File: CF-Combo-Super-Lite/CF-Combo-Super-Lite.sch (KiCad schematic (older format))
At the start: 21 parts, among them J1 IDE_CONNECTOR, J2 CF Adapter Power, J3 Jumpers, J4 Bus_ISA_8bit, U1 BIOS FLASH, U2 74HCT245, U3 GAL22V10, U4 DS1315, U5 AS6C4008-55PCN, Y1 32.768 KHz

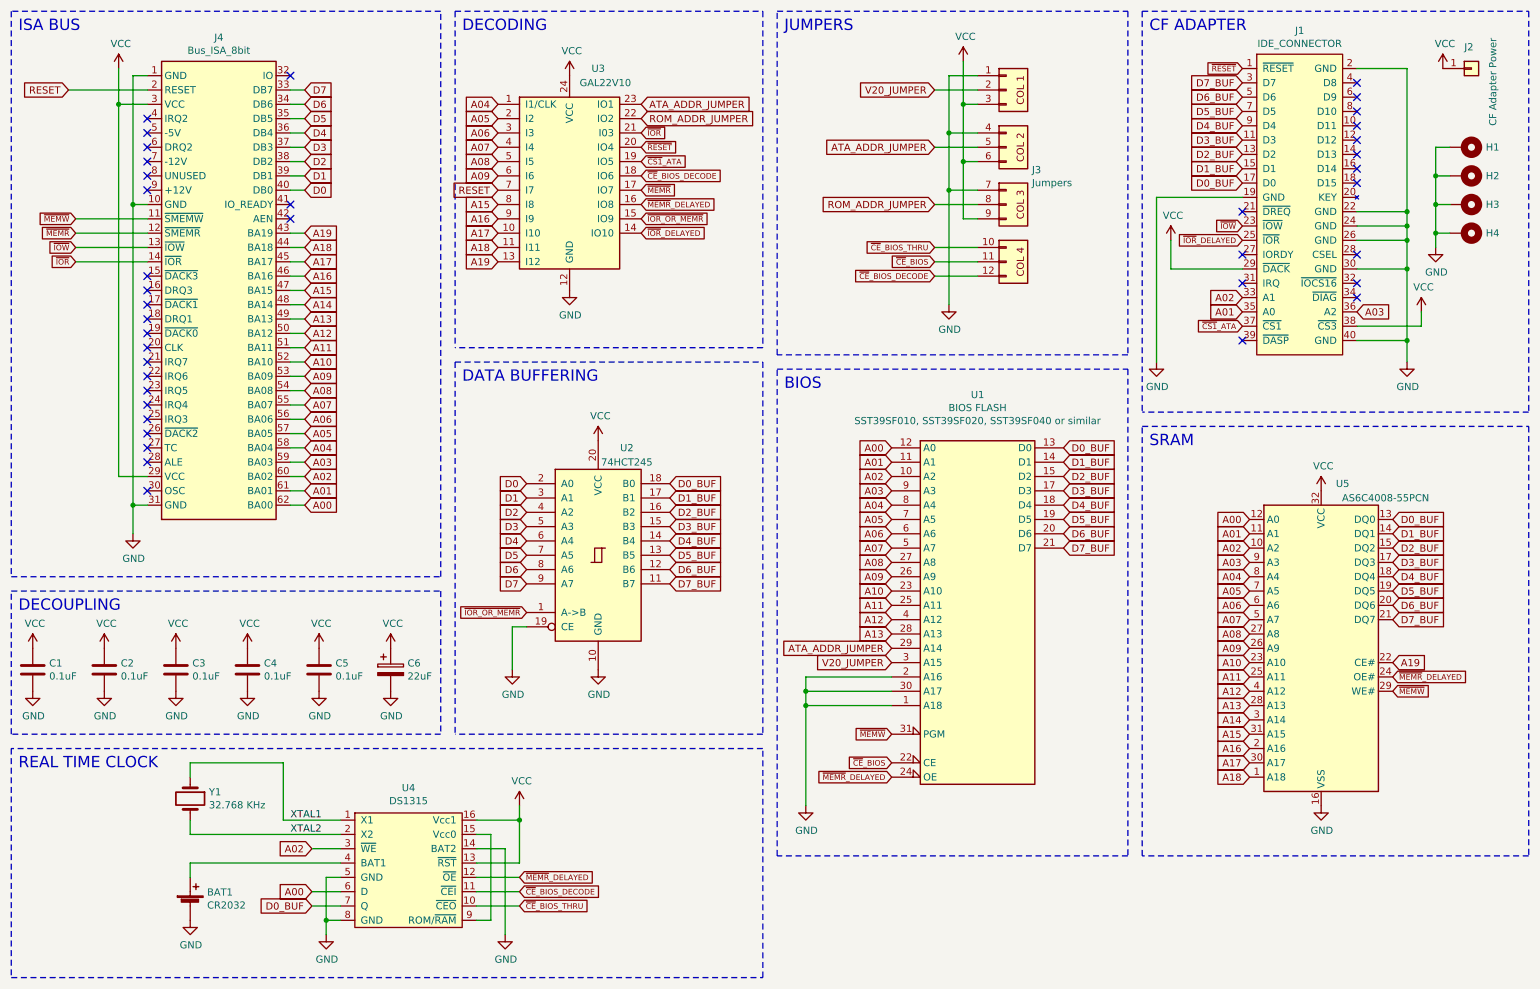
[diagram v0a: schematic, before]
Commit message: CF-Combo-Super-Lite: Note that SmartWatch and clock are optional.
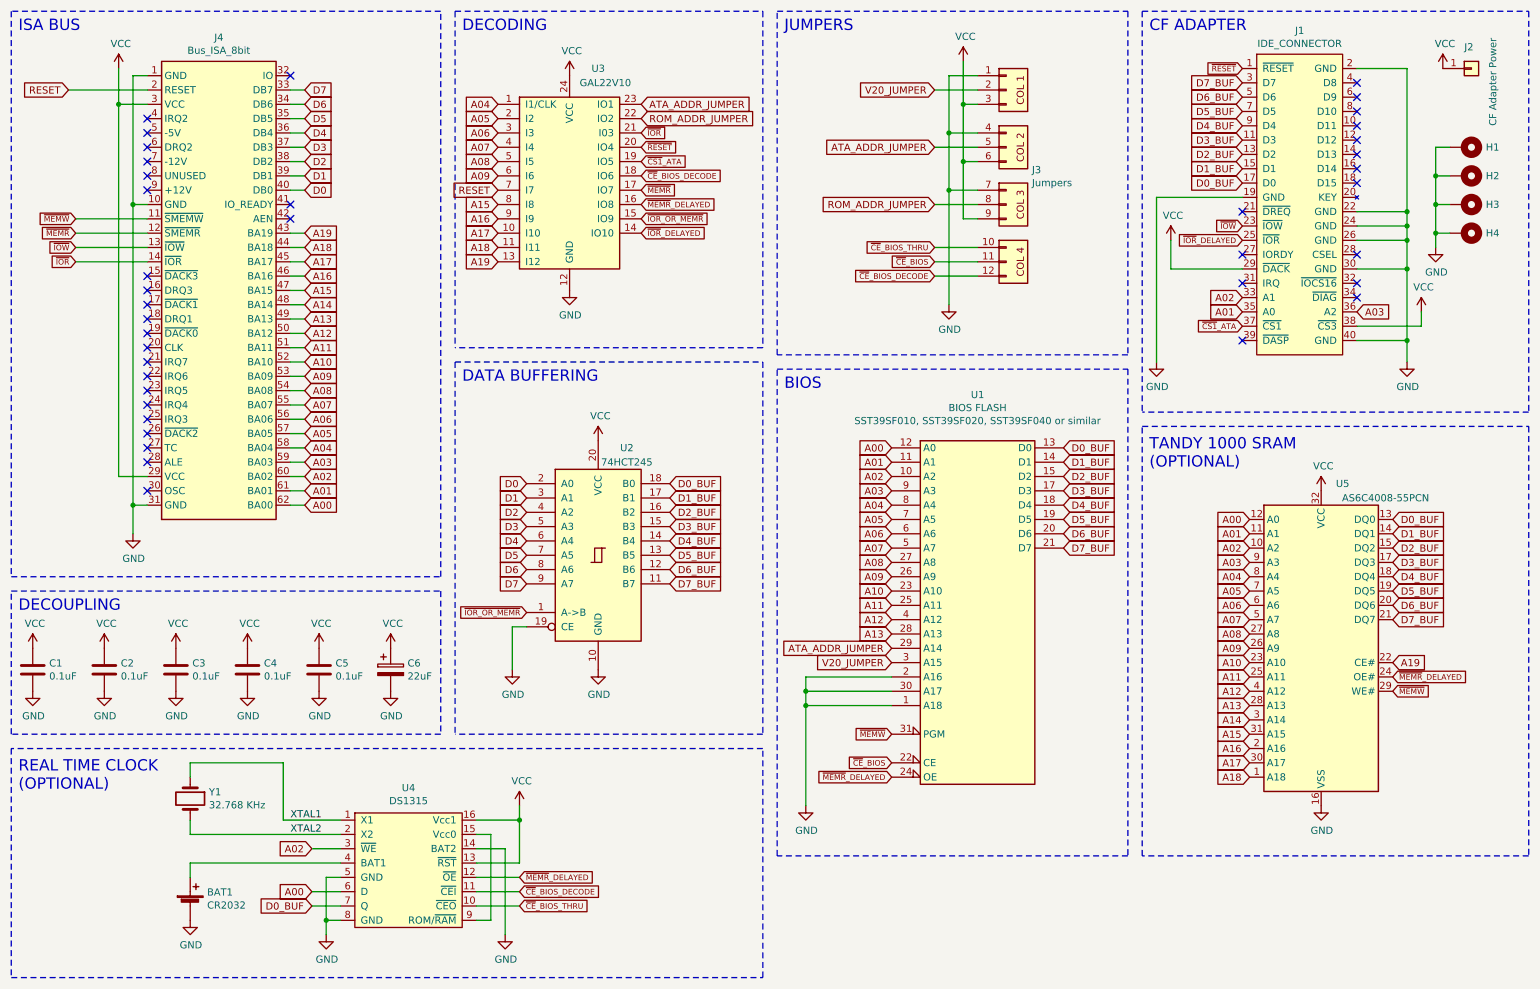
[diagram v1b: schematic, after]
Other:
- note added: "REAL TIME CLOCK\n(OPTIONAL)"
- note added: "TANDY 1000 SRAM\n(OPTIONAL)"
- note removed: "REAL TIME CLOCK"
- note removed: "SRAM"
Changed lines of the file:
@@
 Wire Notes Line
 	5800 5700 550  5700
-Text Notes 600  5850 0    79   ~ 0
-REAL TIME CLOCK
+Text Notes 600  6000 0    79   ~ 0
+REAL TIME CLOCK\n(OPTIONAL)
 $Comp
 L Memory_RAM:AS6C4008-55PCN U5
@@
 Text GLabel 10200 5300 2    39   Input ~ 0
 ~MEMW
-Text Notes 8500 3600 0    79   ~ 0
-SRAM
+Text Notes 8500 3750 0    79   ~ 0
+TANDY 1000 SRAM\n(OPTIONAL)
 Wire Notes Line
 	8450 3450 11150 3450
